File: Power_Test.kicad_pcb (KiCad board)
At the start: 2 copper layers, 67.7 x 59.6 mm, 50 parts, among them J1 Conn_01x01, J2 Conn_01x01, J3 Conn_01x01, J4 Conn_01x01, J5 Conn_01x01, J6 Conn_01x01, J7 Conn_02x05_Odd_Even, J8 Conn_02x05_Odd_Even, Q1 C2M0280120D, Q2 C2M0280120D, Q3 C2M0280120D, Q4 C2M0280120D, Q5 C2M0280120D, Q6 C2M0280120D

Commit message: VER1.0: добавил 4 транзистор
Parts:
- removed the J5 at (179.2, 155.5)
- removed the J6 at (179.2, 161.0)
- removed the R18 at (164.8, 127.0)
- removed the R19 at (164.8, 124.5)
- removed the R20 at (167.5, 117.2)
- removed the R3 at (193.8, 118.5)
- removed the R4 at (193.8, 116.0)
- removed the R5 at (191.2, 126.0)
- added C7: 10n, Capacitor_SMD:C_0805_2012Metric_Pad1.18x1.45mm_HandSolder, F.Cu at (191.2, 111.5)
- added C8: 10n, Capacitor_SMD:C_0805_2012Metric_Pad1.18x1.45mm_HandSolder, F.Cu at (167.5, 98.5)
- added D1: STTH1R06A, Diode_SMD:D_SMA_Handsoldering, B.Cu at (192.2, 165.5)
- added D2: STTH1R06A, Diode_SMD:D_SMA_Handsoldering, B.Cu at (187.2, 169.0)
- added D3: STTH1R06A, Diode_SMD:D_SMA_Handsoldering, B.Cu at (166.0, 165.5)
- added D4: STTH1R06A, Diode_SMD:D_SMA_Handsoldering, B.Cu at (171.0, 169.0)
- added Q7: C2M0280120D, Package_TO_SOT_THT:TO-247-3_Horizontal_TabUp, B.Cu at (186.1, 99.5)
- added Q8: C2M0280120D, Package_TO_SOT_THT:TO-247-3_Horizontal_TabUp, B.Cu at (172.2, 110.5)
- R10: renamed from R30; value 10k -> 15; footprint Resistor_SMD:R_0805_2012Metric_Pad1.20x1.40mm_HandSolder -> Resistor_SMD:R_1206_3216Metric_Pad1.30x1.75mm_HandSolder
- R11: renamed from R6; value 15 -> 10k; footprint Resistor_SMD:R_1206_3216Metric_Pad1.30x1.75mm_HandSolder -> Resistor_SMD:R_0805_2012Metric_Pad1.20x1.40mm_HandSolder
- R12: renamed from R22; value 15 -> 10k; footprint Resistor_SMD:R_1206_3216Metric_Pad1.30x1.75mm_HandSolder -> Resistor_SMD:R_0805_2012Metric_Pad1.20x1.40mm_HandSolder
- R15: renamed from R25; value 10k -> 15; footprint Resistor_SMD:R_0805_2012Metric_Pad1.20x1.40mm_HandSolder -> Resistor_SMD:R_1206_3216Metric_Pad1.30x1.75mm_HandSolder
- R17: renamed from R8; value 15 -> 10k; footprint Resistor_SMD:R_1206_3216Metric_Pad1.30x1.75mm_HandSolder -> Resistor_SMD:R_0805_2012Metric_Pad1.20x1.40mm_HandSolder
- R18: renamed from R24; value 15 -> 10k; footprint Resistor_SMD:R_1206_3216Metric_Pad1.30x1.75mm_HandSolder -> Resistor_SMD:R_0805_2012Metric_Pad1.20x1.40mm_HandSolder
- R19: renamed from R10; value 10k -> 15; footprint Resistor_SMD:R_0805_2012Metric_Pad1.20x1.40mm_HandSolder -> Resistor_SMD:R_1206_3216Metric_Pad1.30x1.75mm_HandSolder
- R23: renamed from R2; value 15 -> 10k; footprint Resistor_SMD:R_1206_3216Metric_Pad1.30x1.75mm_HandSolder -> Resistor_SMD:R_0805_2012Metric_Pad1.20x1.40mm_HandSolder
- R24: renamed from R17; value 15 -> 10k; footprint Resistor_SMD:R_1206_3216Metric_Pad1.30x1.75mm_HandSolder -> Resistor_SMD:R_0805_2012Metric_Pad1.20x1.40mm_HandSolder
- R5: renamed from R13; value 15 -> 10k; footprint Resistor_SMD:R_1206_3216Metric_Pad1.30x1.75mm_HandSolder -> Resistor_SMD:R_0805_2012Metric_Pad1.20x1.40mm_HandSolder
- R6: renamed from R28; value 15 -> 10k; footprint Resistor_SMD:R_1206_3216Metric_Pad1.30x1.75mm_HandSolder -> Resistor_SMD:R_0805_2012Metric_Pad1.20x1.40mm_HandSolder
- R8: renamed from R15; value 10k -> 15; footprint Resistor_SMD:R_0805_2012Metric_Pad1.20x1.40mm_HandSolder -> Resistor_SMD:R_1206_3216Metric_Pad1.30x1.75mm_HandSolder
- moved R19 41.1 mm to (193.8, 102.0), turned to 180 degrees
- moved R9 38.6 mm to (193.8, 133.0), turned to 0 degrees
- moved R20 37.9 mm to (165.2, 110.5)
- moved J1 36.8 mm to (179.2, 158.2)
- moved J4 36.2 mm to (179.2, 107.8)
- moved R15 31.8 mm to (193.8, 116.0), turned to 0 degrees
- moved R8 30.4 mm to (165.2, 144.2)
- moved R18 24.7 mm to (167.5, 117.2)
- moved R21 24.1 mm to (193.8, 99.5), turned to 0 degrees
- moved R13 19.6 mm to (193.8, 118.5)
- moved R16 19.5 mm to (165.2, 124.8)
- moved R24 19.0 mm to (167.5, 100.8), turned to 180 degrees
- moved R7 14.8 mm to (193.8, 135.5), turned to 180 degrees
- moved J2 14.2 mm to (179.2, 141.2)
- moved J3 14.2 mm to (179.2, 124.2)
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- renumbered C3 to C1, C6 to C2, C2 to C3, C5 to C4, C1 to C5, C4 to C6, J7 to J5, J8 to J6, Q3 to Q1, Q6 to Q2, Q2 to Q3, Q5 to Q4, Q1 to Q5, Q4 to Q6, R11 to R1, R7 to R13, R21 to R14, R23 to R16, R27 to R2, R9 to R20, R1 to R21, R16 to R22, R12 to R3, R26 to R4, R14 to R7, R29 to R9
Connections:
- J5 pad 10: OUT -> DESAT_L
- J5 pad 3: OutH2 -> OutL2
- J5 pad 4: OutH2 -> OutL2
- J5 pad 9: OUT -> DESAT_L
- J6 pad 1: GNDPWR -> DESAT_H
- J6 pad 2: GNDPWR -> DESAT_H
- J6 pad 3: OutH2 -> ClampL
- J6 pad 4: OutH2 -> ClampL
- J6 pad 5: OutL2 -> OutH1
- J6 pad 6: OutL2 -> OutH1
- J6 pad 7: ClampL -> OutH1
- J6 pad 8: ClampL -> OutH1
- R10 pad 1: GNDPWR -> ClampL
- R10 pad 2: ClampL -> OutL2
- R11 pad 1: OutH1 -> OUT
- R12 pad 1: OutH2 -> GNDPWR
- R14 pad 1: OutH2 -> OutL2
- R15 pad 1: GNDPWR -> ClampH
- R15 pad 2: ClampL -> OutH1
- R17 pad 1: ClampH -> OUT
- R17 pad 2: OutL1 -> ClampH
- R18 pad 1: ClampL -> GNDPWR
- R18 pad 2: OutL2 -> ClampL
- R19 pad 1: OUT -> OutH1
- R2 pad 1: OutH2 -> OutL2
- R20 pad 1: ClampH -> OutL2
- R20 pad 2: OutL1 -> ClampL
- R21 pad 1: OutH1 -> ClampH
- R21 pad 2: ClampH -> OutH1
- R22 pad 1: OutH2 -> ClampL
- R22 pad 2: ClampL -> OutL2
- R23 pad 1: OutH1 -> OUT
- R24 pad 1: OutH2 -> GNDPWR
- R3 pad 1: OutH1 -> ClampH
- R3 pad 2: ClampH -> OutH1
- R4 pad 1: OutH2 -> ClampL
- R4 pad 2: ClampL -> OutL2
- R5 pad 1: ClampH -> OUT
- R5 pad 2: OutL1 -> ClampH
- R6 pad 1: ClampL -> GNDPWR
- R6 pad 2: OutL2 -> ClampL
- R7 pad 1: ClampH -> OutH1
- R7 pad 2: OutL1 -> ClampH
- R8 pad 1: OUT -> OutL2
- R8 pad 2: ClampH -> ClampL
- R9 pad 1: ClampL -> ClampH
- R9 pad 2: OutL2 -> OutH1
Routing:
- net OUT: track 26.0 -> 15.5 mm
- net DESAT_L: track 0.00 -> 8.55 mm
- net DESAT_H: track 0.00 -> 6.33 mm
- net Net-(D3-K): track 0.00 -> 3.50 mm
- net Net-(D1-K): track 0.00 -> 3.50 mm
- net GNDPWR: track 2.54 -> 0.00 mm
- net ClampL: track 12.7 -> 12.1 mm
- net OutH2: vias 12 -> 0
- added copper zone on F.Cu, net ClampH
- added copper zone on F.Cu, net OutH1
- removed copper zone on B.Cu, net OutH2
- removed copper zone on F.Cu, net OutH2
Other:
- board size 67.7 x 59.6 mm -> 67.7 x 74 mm

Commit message: VER1.0: добавил шину
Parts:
- removed D1, D2, D3, D4: STTH1R06A, Diode_SMD:D_SMA_Handsoldering
- added J7: Conn_02x05_Odd_Even, Connector_PinSocket_2.54mm:PinSocket_2x05_P2.54mm_Vertical, F.Cu at (174.2, 165.7)
- moved J4 0.50 mm to (179.2, 107.2)
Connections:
- J5 pad 10: DESAT_L -> unconnected-(J5-Pin_10-Pad10)
- J5 pad 9: DESAT_L -> unconnected-(J5-Pin_9-Pad9)
- J6 pad 1: DESAT_H -> unconnected-(J6-Pin_1-Pad1)
- J6 pad 2: DESAT_H -> unconnected-(J6-Pin_2-Pad2)
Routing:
- net OUT: track 15.5 -> 0.00 mm
- net DESAT_L: track 8.55 -> 0.00 mm
- net (no net): track 0.00 -> 7.92 mm
- net DESAT_H: track 6.33 -> 0.00 mm
- net Net-(D3-K): track 3.50 -> 0.00 mm
- net Net-(D1-K): track 3.50 -> 0.00 mm

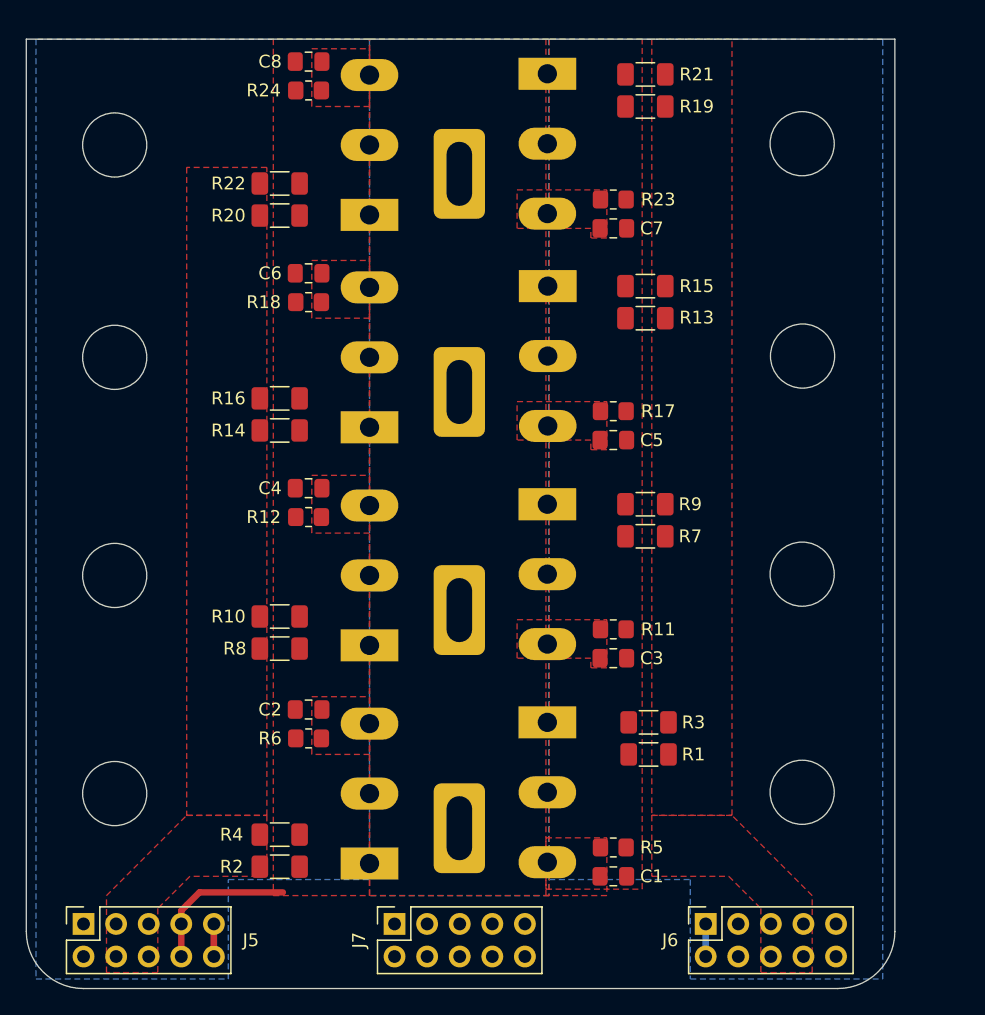
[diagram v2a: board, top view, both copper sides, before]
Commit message: VER1.0: добавил две шины сверху и снизу
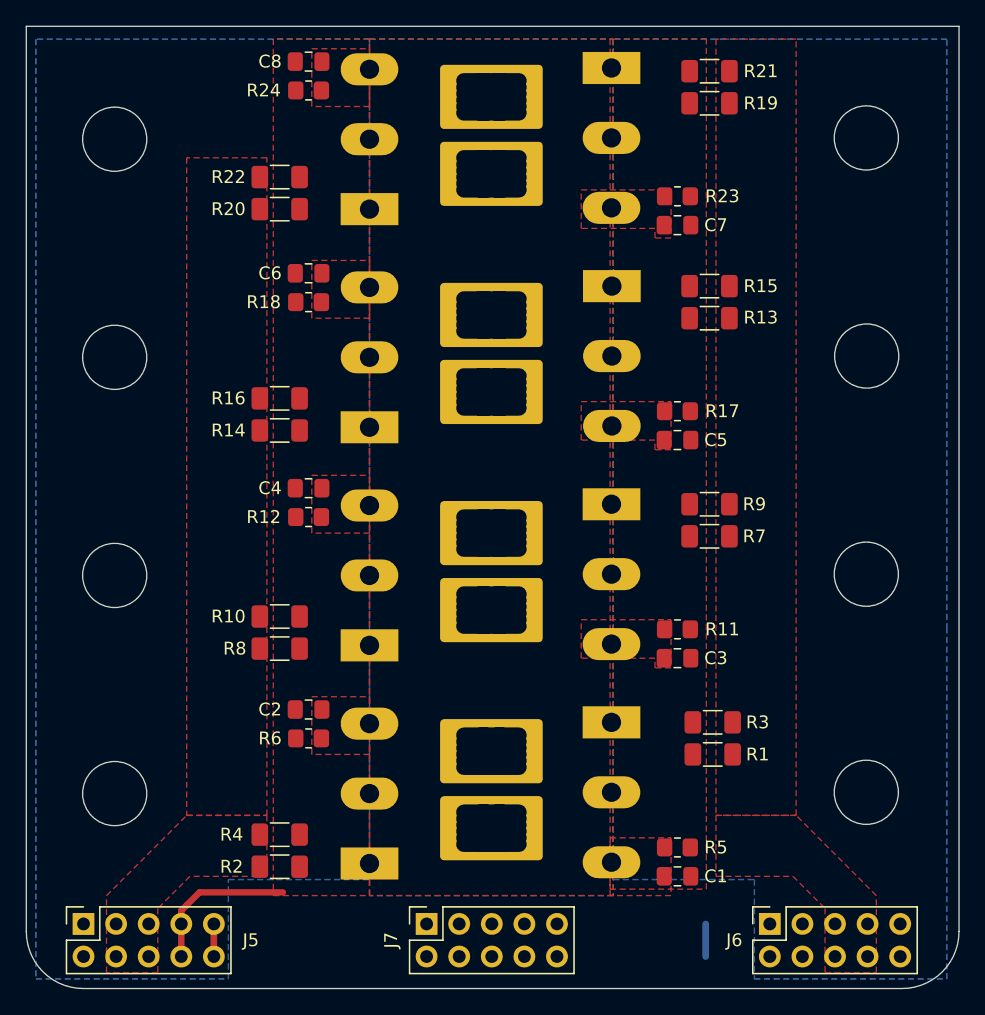
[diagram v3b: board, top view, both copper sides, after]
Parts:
- added J10: Conn_01x01, Bush_my:Bush_5x3, F.Cu at (181.8, 118.2)
- added J11: Conn_01x01, Bush_my:Bush_5x3, F.Cu at (181.8, 101.2)
- added J8: Conn_01x01, Bush_my:Bush_5x3, F.Cu at (181.8, 152.2)
- added J9: Conn_01x01, Bush_my:Bush_5x3, F.Cu at (181.8, 135.2)
- moved Q7 5.02 mm to (191.1, 99.0)
- moved C7 5.01 mm to (196.2, 111.2)
- moved R19 5.01 mm to (198.8, 101.8)
- moved R21 5.01 mm to (198.8, 99.2)
- moved R23 5.01 mm to (196.2, 109.0)
- moved C1 5.00 mm to (196.2, 162.0)
- moved C3 5.00 mm to (196.2, 145.0)
- moved C5 5.00 mm to (196.2, 128.0)
- moved J6 5.00 mm to (203.4, 165.7)
- moved Q1 5.00 mm to (191.1, 150.0)
- moved Q3 5.00 mm to (191.1, 133.0)
- moved Q5 5.00 mm to (191.1, 116.0)
- moved R1 5.00 mm to (199.0, 152.5)
- moved R11 5.00 mm to (196.2, 142.8)
- moved R13 5.00 mm to (198.8, 118.5)
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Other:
- board size 67.7 x 74 mm -> 72.7 x 75 mm

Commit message: VER1.0: пересобрал стойку, добавил разъёмы высоковольтные
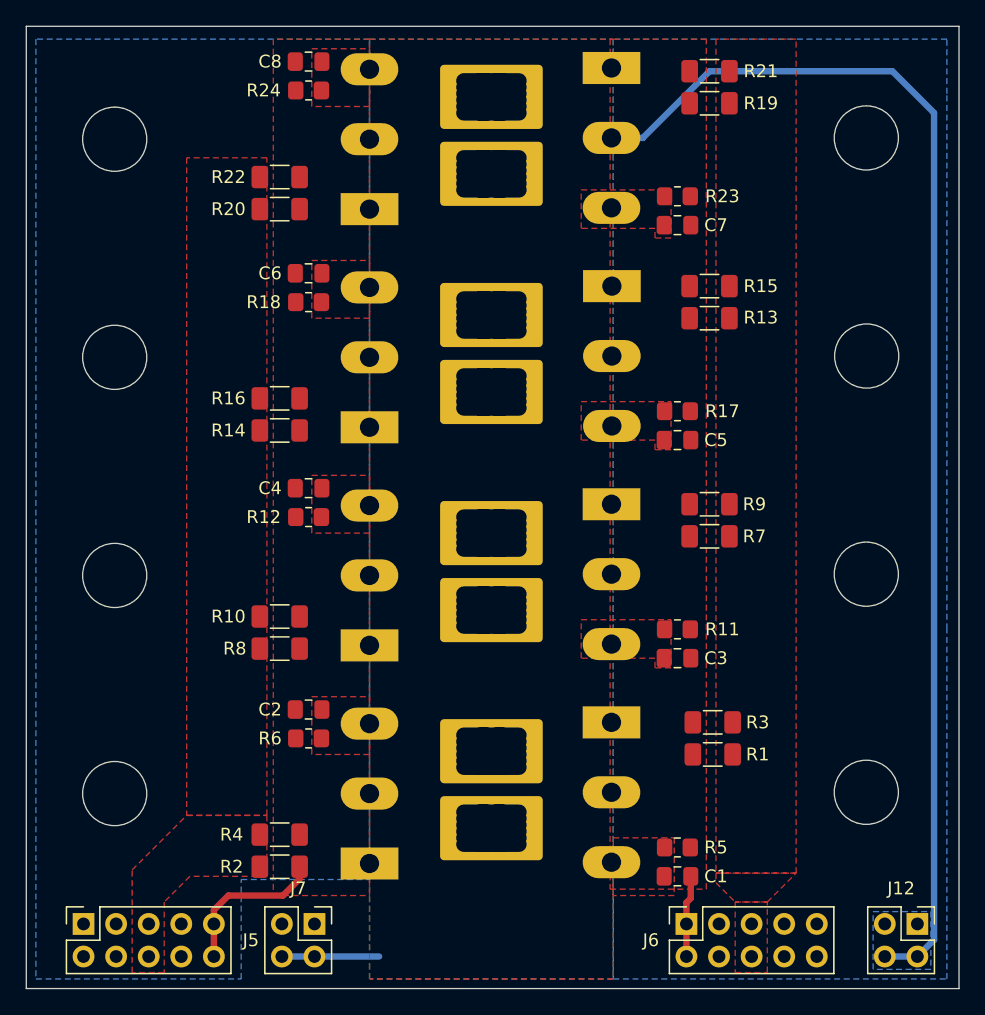
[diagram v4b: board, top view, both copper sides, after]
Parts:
- added J12: Conn_02x02_Odd_Even, Connector_PinSocket_2.54mm:PinSocket_2x02_P2.54mm_Vertical, F.Cu at (214.9, 165.7)
- J7: value Conn_02x05_Odd_Even -> Conn_02x02_Odd_Even; footprint Connector_PinSocket_2.54mm:PinSocket_2x05_P2.54mm_Vertical -> Connector_PinSocket_2.54mm:PinSocket_2x02_P2.54mm_Vertical
- moved J7 8.74 mm to (168.0, 165.7), turned to 0 degrees
- moved J6 6.50 mm to (196.9, 165.7)
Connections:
- J5 pad 1: GNDPWR -> ClampL
- J5 pad 10: unconnected-(J5-Pin_10-Pad10) -> ClampL
- J5 pad 2: GNDPWR -> ClampL
- J5 pad 3: OutL2 -> GNDPWR
- J5 pad 4: OutL2 -> GNDPWR
- J5 pad 7: ClampL -> GNDPWR
- J5 pad 8: ClampL -> GNDPWR
- J5 pad 9: unconnected-(J5-Pin_9-Pad9) -> ClampL
- J6 pad 1: unconnected-(J6-Pin_1-Pad1) -> ClampH
- J6 pad 10: OUT -> ClampH
- J6 pad 2: unconnected-(J6-Pin_2-Pad2) -> ClampH
- J6 pad 3: ClampL -> OUT
- J6 pad 4: ClampL -> OUT
- J6 pad 7: OutH1 -> OUT
- J6 pad 8: OutH1 -> OUT
- J6 pad 9: OUT -> ClampH
- J7 pad 3: unconnected-(J7-Pin_3-Pad3) -> OUT
- J7 pad 4: unconnected-(J7-Pin_4-Pad4) -> OUT
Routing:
- net VDC: track 0.00 -> 97.5 mm
- net (no net): track 7.92 -> 0.00 mm
- net OUT: track 0.00 -> 7.58 mm
- net ClampH: track 0.00 -> 6.39 mm
- added copper zone on B.Cu, net VDC
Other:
- outline, holes or cut-outs redrawn
